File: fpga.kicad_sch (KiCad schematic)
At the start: 0 parts

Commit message: schematics done
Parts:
- added C3, C35, C38, C39, C41, C42, C44, C45, C47, C48, C50, C51, C52: 100n, Capacitor_SMD:C_0603_1608Metric_Pad1.08x0.95mm_HandSolder, symbol Device:C
- added C34: 1n, Capacitor_SMD:C_0603_1608Metric_Pad1.08x0.95mm_HandSolder, symbol Device:C
- added C36, C37, C40, C43, C46, C49: 1u, Capacitor_SMD:C_0603_1608Metric_Pad1.08x0.95mm_HandSolder, symbol Device:C
- added C4: 10n, Capacitor_SMD:C_0603_1608Metric, symbol Device:C
- added D10, D11, D12, D13, D14, D15, D16, D17, D18, D19, D20, D21, D22, D23, D25, D7, D8, D9: BAT54S, Package_TO_SOT_SMD:SOT-23, symbol Diode:BAT54S
- added NT1, NT2, NT3, NT4, NT5, NT6, NT7, NT8: NetTie_2, symbol Device:NetTie_2
- added R60, R62, R63, R64, R65: 100, Capacitor_SMD:C_0603_1608Metric_Pad1.08x0.95mm_HandSolder, symbol Device:R
- added R61: 10k, Resistor_SMD:R_0603_1608Metric, symbol Device:R
- added U1: MACHXO2-1200HC-4TG100C, Package_QFP:TQFP-100_14x14mm_P0.5mm, symbol 10_ICs:LCMXO2-1200HC-4TG100C
- added U16: ~, symbol 10_ICs:23AA02M-I/SN
- added U2: TDC_7200, Package_SO:TSSOP-14_4.4x5mm_P0.65mm, symbol 10_ICs:TDC_7200
- added X1: 16MHz, Crystal:Crystal_SMD_5032-4Pin_5.0x3.2mm, symbol 06_oscilators:DSC1001_16MHz
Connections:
- new net: C36.1, U2.13 (VREG)
- new net ADC_CLK: U1.62 (PR5D/PCLKC1_0)
- new net ADC_D0: U1.75 (PR2A)
- new net ADC_D1: U1.74 (PR2B)
- new net ADC_D2: U1.71 (PR3A)
- new net ADC_D3: U1.70 (PR3B)
- new net ADC_D4: U1.69 (PR4A)
- new net ADC_D5: U1.68 (PR4B)
- new net ADC_D6: U1.67 (PR4C)
- new net ADC_D7: U1.66 (PR4D)
- new net ADC_D8: U1.65 (PR5A)
- new net ADC_D9: U1.64 (PR4B)
- new net ADC_DF: U1.63 (PR5C/PCLKT1_0)
- new net ADC_STBY: U1.61 (PR8A)
- new net BRIDGE_A_HI: U1.20 (PL9A/PCLKT3_0)
- new net BRIDGE_A_LO: U1.21 (PL9B/PCLKC3_0)
- new net BRIDGE_B_HI: U1.24 (PL10C)
- new net BRIDGE_B_LO: U1.25 (PL10D)
- new net BRIDGE_C_HI: U1.27 (PB4C/CSSPIN)
- new net BRIDGE_C_LO: U1.28 (PB4D)
- new net BRIDGE_D_HI: U1.29 (PB6A), U1.30 (PB6B)
- new net CLK: U1.1 (PL2C/L_GPLLT_IN), U2.5 (CLOCK), X1.3 (OUT)
- new net CNTRL_CS: D16.3 (COM), U1.48 (PB20C/SN)
- new net CNTRL_GPIO0: D25.3 (COM), U1.76 (PT17D/DONE)
- new net CNTRL_GPIO1: D23.3 (COM), U1.77 (PT17C/INITN)
- new net CNTRL_GPIO2: D22.3 (COM), R60.2, U1.81 (PT15D/PROGRAMN)
- new net CNTRL_GPIO3: D20.3 (COM), U1.82 (PT15C/JTAGENB)
- new net CNTRL_GPIO4: D21.3 (COM), U1.85 (PT12D/SDA/PCLKC0_0)
- new net CNTRL_GPIO5: D19.3 (COM), U1.86 (PT12C/SCL/PCLKT0_0)
- new net CNTRL_MISO: D17.3 (COM), U1.32 (PB6D/SO/SPISO)
- new net CNTRL_MOSI: D18.3 (COM), U1.49 (PB20D/SI/SISPI)
- new net CNTRL_SCLK: D14.3 (COM), U1.31 (PB6C/MCLK/CCLK)
- new net DAC_CS: U1.14 (PL5C)
- new net DAC_MOSI: NT1.2
- new net DAC_SCLK: NT3.2
- new net EN_HV_REGULATOR: U1.19 (PL8D)
- new net EN_SIGNAL_B: U1.99 (PT9A)
- new net EN_SIGNAL_D: U1.98 (PT9B)
- new net GND: C3.1, C34.2, C35.2, C36.2, C37.1, C38.1, C39.1, C4.1, C40.1, C41.1, C42.1, C43.1, C44.1, C45.1, C46.1, C47.1, C48.1, C49.1, C50.1, C51.1, C52.1, D10.1 (A), D11.1 (A), D12.1 (A), D13.1 (A), D14.1 (A), D15.1 (A), D16.1 (A), D17.1 (A), D18.1 (A), D19.1 (A), D20.1 (A), D21.1 (A), D22.1 (A), D23.1 (A), D25.1 (A), D7.1 (A), D8.1 (A), D9.1 (A), U1.22 (GND), U1.33 (GND), U1.44 (GND), U1.56 (GND), U1.6 (GND), U1.72 (GND), U1.79 (GND), U1.92 (GND), U16.4 (VSS), U2.7 (GND), X1.2 (GND)
- new net JTAG_TCK: U1.91 (PT11C/TCK)
- new net JTAG_TDI: U1.94 (PT10D/TDI)
- new net JTAG_TDO: U1.95 (PT10C/TDO)
- new net JTAG_TMS: U1.90 (PT11D/TMS)
- new net LVDS_CS_N: D9.3 (COM), R63.2, U1.57 (PR9B)
- new net LVDS_CS_P: D11.3 (COM), R63.1, U1.58 (PR9A)
- new net LVDS_MISO_N: D10.3 (COM), R64.2, U1.53 (PR9D)
- new net LVDS_MISO_P: D13.3 (COM), R64.1, U1.54 (PR9C)
- new net LVDS_MOSI_N: D12.3 (COM), R65.2, U1.51 (PR10D)
- new net LVDS_MOSI_P: D15.3 (COM), R65.1, U1.52 (PR10C)
- new net LVDS_SCLK_N: D7.3 (COM), R62.2, U1.59 (PR8D)
- new net LVDS_SCLK_P: D8.3 (COM), R62.1, U1.60 (PR8C)
- new net P3V3: C3.2, C34.1, C35.1, C37.2, C38.2, C39.2, C4.2, C40.2, C41.2, C42.2, C43.2, C44.2, C45.2, C46.2, C47.2, C48.2, C49.2, C50.2, C51.2, C52.2, D10.2 (K), D11.2 (K), D12.2 (K), D13.2 (K), D14.2 (K), D15.2 (K), D16.2 (K), D17.2 (K), D18.2 (K), D19.2 (K), D20.2 (K), D21.2 (K), D22.2 (K), D23.2 (K), D25.2 (K), D7.2 (K), D8.2 (K), D9.2 (K), R60.1, R61.1, U1.100 (VCC), U1.11 (VCCIO3), U1.23 (VCCIO3), U1.26 (VCCIO2), U1.46 (VCCIO2), U1.5 (VCCIO3), U1.50 (VCC), U1.55 (VCCIO1), U1.73 (VCCIO1), U1.80 (VCCIO0), U1.93 (VCCIO0), U16.8 (VCC), U2.14 (VDD), X1.4 (VCC)
- new net PGA_GATE0: U1.35 (PB9B/PCLKC2_0)
- new net PGA_GATE1: U1.38 (PB11A/PCLKT2_1)
- new net PGA_GATE2: U1.39 (PB11B/PCLKC2_1)
- new net PGA_GATE20: U1.41 (PB15B)
- new net PGA_GATE21: U1.42 (PB18A)
- new net PGA_GATE22: U1.43 (PB18B)
- new net PGA_GATE23: U1.45 (PB18C)
- new net PGA_GATE24: U1.47 (PB18D)
- new net PGA_GATE3: U1.36 (PB11C)
- new net PGA_GATE4: U1.37 (PB11D)
- new net PGOOD_HV_REGULATOR: U1.18 (PL8C)
- new net SPI_LOCAL_MISO: NT2.1, NT8.1, U1.17 (PL8B)
- new net SPI_LOCAL_MOSI: NT1.1, NT5.1, NT7.1, U1.16 (PL8A)
- new net SPI_LOCAL_SCK: NT3.1, NT4.1, NT6.1, U1.12 (PL5A/PCLKT3_1)
- new net SRAM_CS: U1.15 (PL5D), U16.1 (CS)
- new net SRAM_MISO: NT8.2, U16.2 (SO/SIO1)
- new net SRAM_MOSI: NT7.2, U16.5 (SI/SIO0)
- new net SRAM_SCLK: NT6.2, U16.6 (SCK)
- new net STANBY_OSC: R61.2, U1.78 (PT16C), X1.1 (Standby)
- new net STOP_SIGNAL: U1.97 (PT10A)
- new net TDC_CS: U1.13 (PL5B/PCLKC3_1), U2.11 (CSB)
- new net TDC_EN: U1.9 (PL4A), U2.1 (ENABLE)
- new net TDC_INTB: U1.10 (PL4B), U2.8 (INTB)
- new net TDC_MISO: NT2.2, U2.9 (DOUT)
- new net TDC_MOSI: NT5.2, U2.10 (DIN)
- new net TDC_SCLK: NT4.2, U2.12 (SCLK)
- new net TDC_START: U1.7 (PL3C), U2.3 (START)
- new net TDC_STOP: U1.4 (PL3B/PCLKC3_2), U2.4 (STOP)
- new net TDC_TRIGG: U1.8 (PL3D), U2.2 (TRIGG)
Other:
- note added: "Add external SRAM for ADC data coming out of FIFO buffer DONE Connect the LVDS signals DONE Add 16MHz oscilator DONE Add shottky diode protection DONE Clean up schematic"

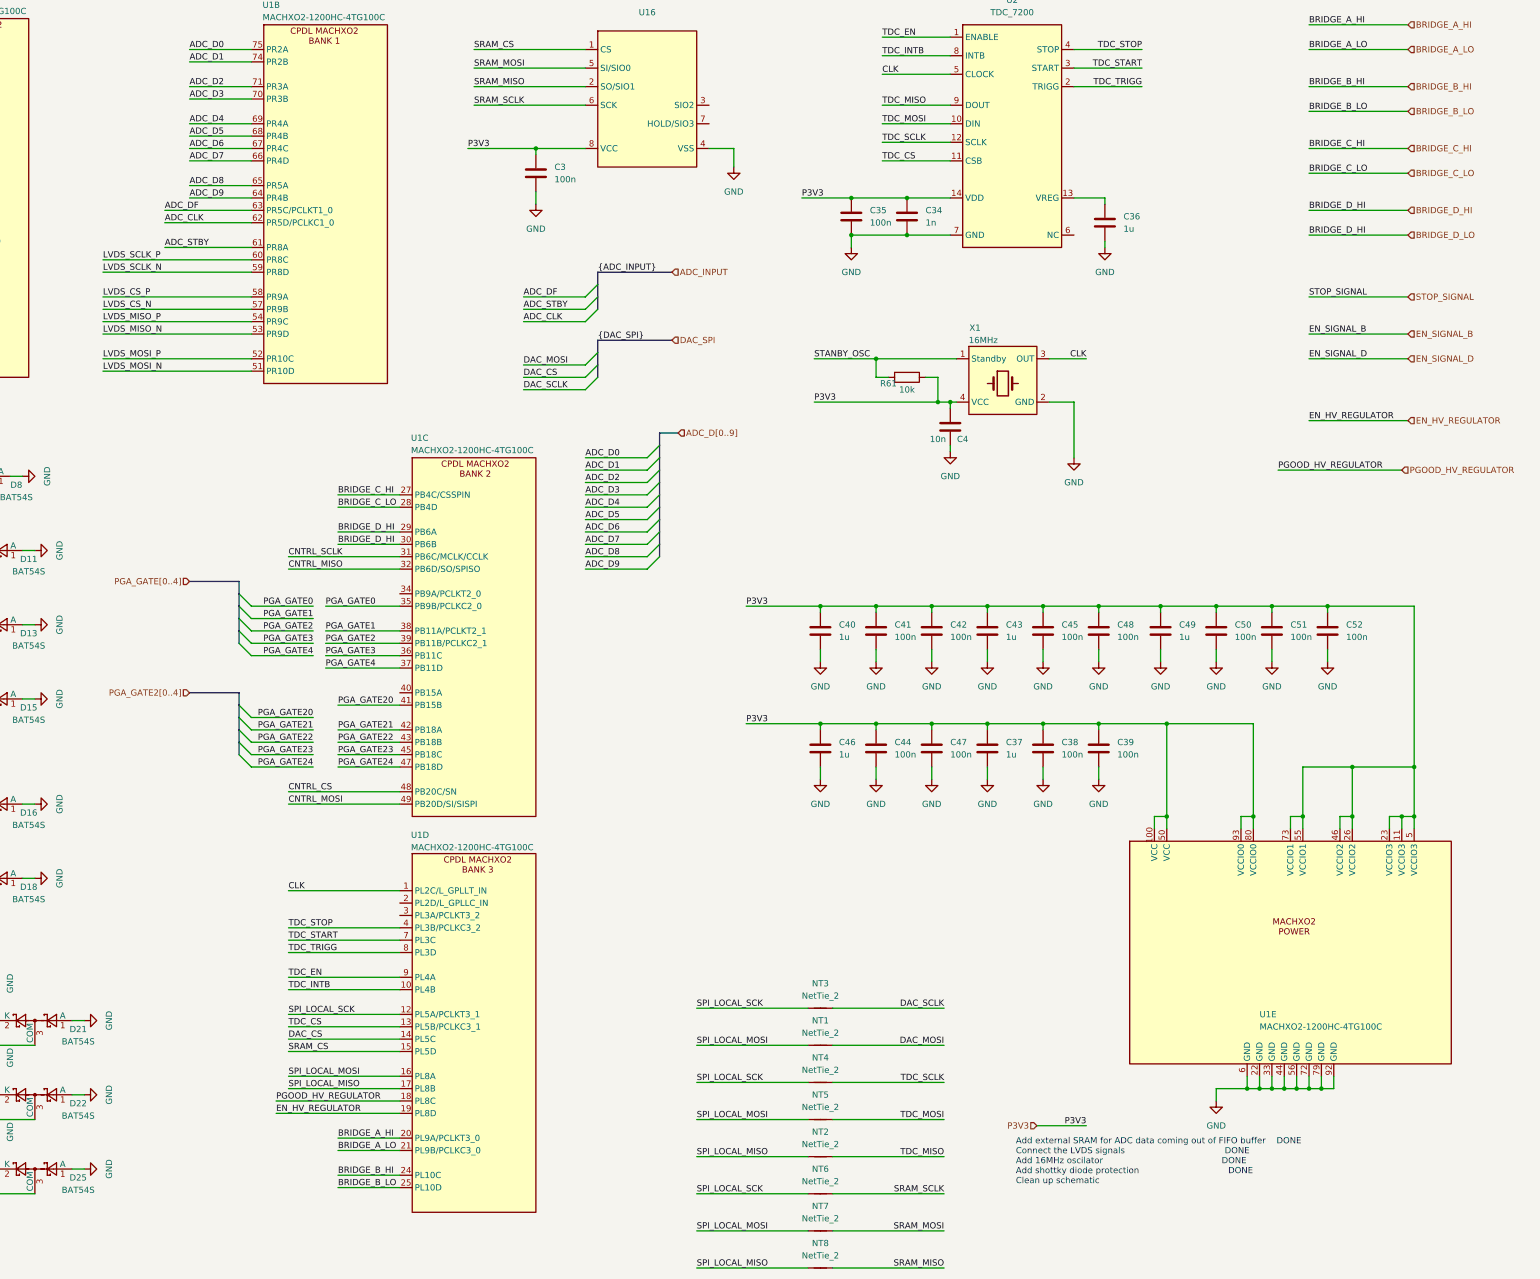
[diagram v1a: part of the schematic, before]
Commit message: ready schematic for layout
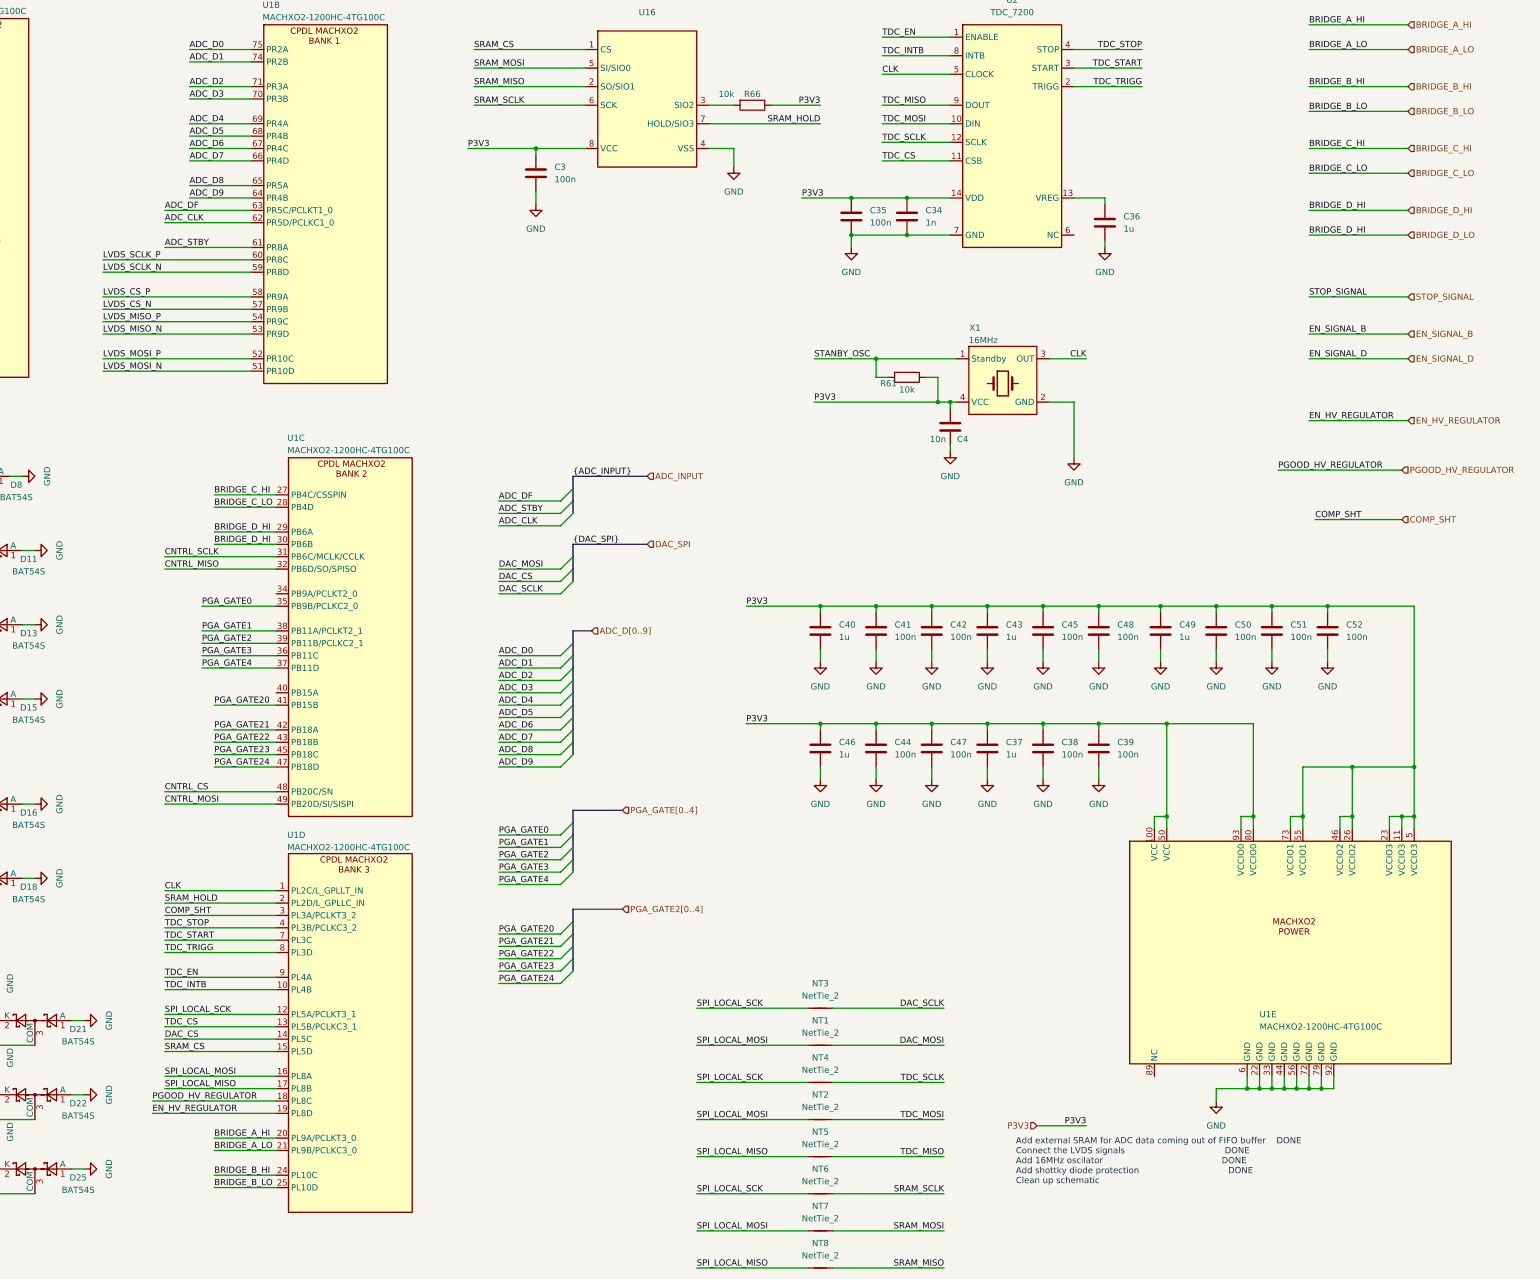
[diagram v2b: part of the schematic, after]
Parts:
- added R66: 10k, Resistor_SMD:R_0603_1608Metric, symbol Device:R
- NT1, NT2, NT3, NT4, NT5, NT6, NT7, NT8: footprint (none) -> NetTie:NetTie-2_SMD_Pad0.5mm
- U16: footprint (none) -> Package_SO:SOIC-8_3.9x4.9mm_P1.27mm
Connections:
- net P3V3: now also R66.1
- net SPI_LOCAL_MISO: now also NT5.1; no longer NT2.1
- net SPI_LOCAL_MOSI: now also NT2.1; no longer NT5.1
- net TDC_MISO: now also NT5.2; no longer NT2.2
- net TDC_MOSI: now also NT2.2; no longer NT5.2
- net at U16.3 (SIO2): now also R66.2
- net SRAM_HOLD: now reaches U16.7 (HOLD/SIO3)
- net SRAM_HOLD: now also U1.2 (PL2D/L_GPLLC_IN)
- net COMP_SHT: now reaches U1.3 (PL3A/PCLKT3_2)
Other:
- moved on the sheet: U1C, U1D

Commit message: new analog front end
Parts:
- removed NT1, NT2, NT3, NT4, NT5, NT6, NT7, NT8: NetTie_2, NetTie:NetTie-2_SMD_Pad0.5mm, symbol Device:NetTie_2
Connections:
- net PGA_GATE1 is gone; now on net TDC_CS: U1.38 (PB11A/PCLKT2_1)
- net PGA_GATE2 is gone; now on net DAC_CS: U1.39 (PB11B/PCLKC2_1)
- net PGA_GATE22 is gone; now on net EN_SIGNAL_B: U1.43 (PB18B)
- net PGA_GATE24 is gone; now on net EN_SIGNAL_D: U1.47 (PB18D)
- net PGA_GATE3 is gone; now on net SRAM_CS: U1.36 (PB11C)
- net SRAM_MISO is gone; now on net SPI_LOCAL_MISO: U16.2 (SO/SIO1)
- net SRAM_MOSI is gone; now on net SPI_LOCAL_MOSI: U16.5 (SI/SIO0)
- net SRAM_SCLK is gone; now on net SPI_LOCAL_SCK: U16.6 (SCK)
- net TDC_MISO is gone; now on net SPI_LOCAL_MISO: U2.9 (DOUT)
- net TDC_MOSI is gone; now on net SPI_LOCAL_MOSI: U2.10 (DIN)
- net TDC_SCLK is gone; now on net SPI_LOCAL_SCK: U2.12 (SCLK)
- net DAC_CS: no longer U1.14 (PL5C)
- net EN_SIGNAL_B: no longer U1.99 (PT9A)
- net EN_SIGNAL_D: no longer U1.98 (PT9B)
- net SRAM_CS: no longer U1.15 (PL5D)
- net TDC_CS: no longer U1.13 (PL5B/PCLKC3_1)
- net PGA_GATE0: no longer names the net of U1.35 (PB9B/PCLKC2_0)
- net PGA_GATE20: no longer names the net of U1.41 (PB15B)
- net PGA_GATE21 renamed EN_SIGNAL_A
- net PGA_GATE23 renamed EN_SIGNAL_C
- net PGA_GATE4 renamed AMP_CS
